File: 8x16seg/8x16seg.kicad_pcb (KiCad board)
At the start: 4 copper layers, 162.2 x 30.5 mm, 76 parts, among them P1 CONN_01X08, P2 CONN_01X08, U1 TLC59282_REV, U2 TLC59282_REV, U3 TLC59282_REV, U4 TLC59282_REV, U5 TLC59282_REV, U6 TLC59282_REV, U7 TLC59282_REV, U8 TLC59282_REV, U9 TLC59282_REV

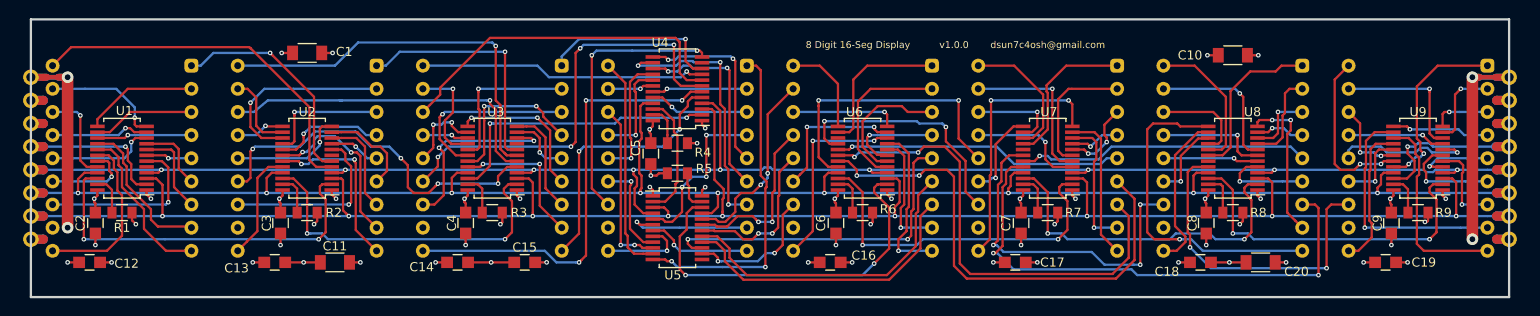
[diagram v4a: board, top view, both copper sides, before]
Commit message: Update 8x16seg design to KiCad 8.
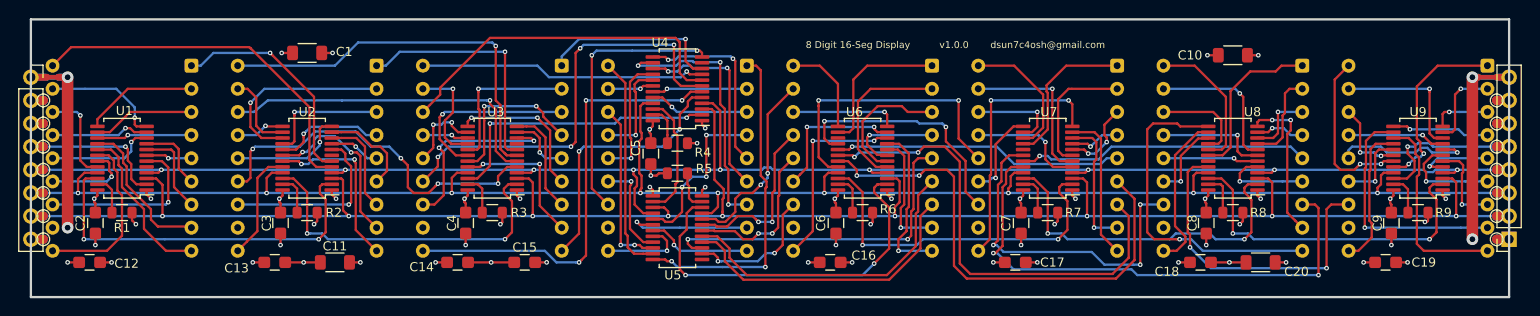
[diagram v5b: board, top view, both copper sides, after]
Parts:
- removed the REF** at (227.1, 97.8) (x2)
- removed the REF** at (227.1, 100.3) (x2)
- removed the REF** at (227.1, 102.9) (x2)
- removed the REF** at (227.1, 105.4) (x2)
- removed the REF** at (227.1, 108.0) (x2)
- removed the REF** at (227.1, 110.5) (x2)
- removed the REF** at (67.6, 110.5) (x2)
- removed the REF** at (227.1, 95.2) (x2)
- removed the REF** at (67.6, 108.0) (x2)
- removed the REF** at (67.6, 105.4) (x2)
- removed the REF** at (67.6, 102.9) (x2)
- removed the REF** at (67.6, 100.3) (x2)
- removed the REF** at (67.6, 97.8) (x2)
- added REF**: TestPoint_Pad_D1.0mm, TestPoint:TestPoint_Pad_D1.0mm, F.Cu at (227.1, 108.0)
- added REF**: TestPoint_Pad_D1.0mm, TestPoint:TestPoint_Pad_D1.0mm, F.Cu at (227.1, 100.3)
- added REF**: TestPoint_Pad_D1.0mm, TestPoint:TestPoint_Pad_D1.0mm, F.Cu at (67.6, 105.4)
- added REF**: TestPoint_Pad_D1.0mm, TestPoint:TestPoint_Pad_D1.0mm, F.Cu at (67.6, 102.9)
- added REF**: TestPoint_Pad_D1.0mm, TestPoint:TestPoint_Pad_D1.0mm, F.Cu at (67.6, 97.8)
- added REF**: TestPoint_Pad_D1.0mm, TestPoint:TestPoint_Pad_D1.0mm, B.Cu at (67.6, 110.5)
- added REF**: TestPoint_Pad_D1.0mm, TestPoint:TestPoint_Pad_D1.0mm, B.Cu at (67.6, 105.4)
- added REF**: TestPoint_Pad_D1.0mm, TestPoint:TestPoint_Pad_D1.0mm, B.Cu at (67.6, 97.8)
- added REF**: TestPoint_Pad_D1.0mm, TestPoint:TestPoint_Pad_D1.0mm, B.Cu at (227.1, 102.9)
- added REF**: TestPoint_Pad_D1.0mm, TestPoint:TestPoint_Pad_D1.0mm, F.Cu at (227.1, 105.4)
- added REF**: TestPoint_Pad_D1.0mm, TestPoint:TestPoint_Pad_D1.0mm, B.Cu at (67.6, 100.3)
- added REF**: TestPoint_Pad_D1.0mm, TestPoint:TestPoint_Pad_D1.0mm, B.Cu at (227.1, 110.5)
- added REF**: TestPoint_Pad_D1.0mm, TestPoint:TestPoint_Pad_D1.0mm, B.Cu at (227.1, 97.8)
- added REF**: TestPoint_Pad_D1.0mm, TestPoint:TestPoint_Pad_D1.0mm, B.Cu at (227.1, 95.2)
- added REF**: TestPoint_Pad_D1.0mm, TestPoint:TestPoint_Pad_D1.0mm, B.Cu at (227.1, 108.0)
- added REF**: TestPoint_Pad_D1.0mm, TestPoint:TestPoint_Pad_D1.0mm, B.Cu at (227.1, 105.4)
- added REF**: TestPoint_Pad_D1.0mm, TestPoint:TestPoint_Pad_D1.0mm, B.Cu at (67.6, 108.0)
- added REF**: TestPoint_Pad_D1.0mm, TestPoint:TestPoint_Pad_D1.0mm, B.Cu at (67.6, 102.9)
- added REF**: TestPoint_Pad_D1.0mm, TestPoint:TestPoint_Pad_D1.0mm, B.Cu at (227.1, 100.3)
- added REF**: TestPoint_Pad_D1.0mm, TestPoint:TestPoint_Pad_D1.0mm, F.Cu at (227.1, 102.9)
- added REF**: TestPoint_Pad_D1.0mm, TestPoint:TestPoint_Pad_D1.0mm, F.Cu at (227.1, 110.5)
- added REF**: TestPoint_Pad_D1.0mm, TestPoint:TestPoint_Pad_D1.0mm, F.Cu at (67.6, 110.5)
- added REF**: TestPoint_Pad_D1.0mm, TestPoint:TestPoint_Pad_D1.0mm, F.Cu at (227.1, 95.2)
- added REF**: TestPoint_Pad_D1.0mm, TestPoint:TestPoint_Pad_D1.0mm, F.Cu at (67.6, 108.0)
- added REF**: TestPoint_Pad_D1.0mm, TestPoint:TestPoint_Pad_D1.0mm, F.Cu at (227.1, 97.8)
- added REF**: TestPoint_Pad_D1.0mm, TestPoint:TestPoint_Pad_D1.0mm, F.Cu at (67.6, 100.3)
- C1, C10, C11, C20: footprint local:C_1206_HandSoldering -> Local:C_1206_HandSoldering
- C12, C13, C14, C15, C16, C17, C18, C19, C2, C3, C4, C5, C6, C7, C8, C9: footprint local:C_0805_HandSoldering -> Local:C_0805_HandSoldering
- DS1, DS2, DS3, DS4, DS5, DS6, DS7, DS8: footprint local:PSA08-11SRWA -> Local:PSA08-11SRWA
- R1, R2, R3, R4, R5, R6, R7, R8, R9: footprint local:R_0805_HandSoldering -> Local:R_0805_HandSoldering
- U1, U2, U3, U4, U5, U6, U7, U8, U9: footprint local:SSOP-24_3.9x8.65mm_Pitch0.635mm -> Local:SSOP-24_3.9x8.65mm_Pitch0.635mm
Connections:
- U1 pad 5: Net-(U1-Pad5) -> unconnected-(U1-OUT0-Pad5)
- U2 pad 7: Net-(U2-Pad7) -> unconnected-(U2-OUT2-Pad7)
- U3 pad 9: Net-(U3-Pad9) -> unconnected-(U3-OUT4-Pad9)
- U4 pad 11: Net-(U4-Pad11) -> unconnected-(U4-OUT6-Pad11)
- U5 pad 13: Net-(U5-Pad13) -> unconnected-(U5-OUT8-Pad13)
- U6 pad 15: Net-(U6-Pad15) -> unconnected-(U6-OUT10-Pad15)
- U7 pad 17: Net-(U7-Pad17) -> unconnected-(U7-OUT12-Pad17)
- U8 pad 19: Net-(U8-Pad19) -> unconnected-(U8-OUT14-Pad19)
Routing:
- net VAA: track 66.9 -> 79.0 mm
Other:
- net class Default removed
- net class minimum removed
- rule solder_mask_min_width: 0.25 -> 0.1016

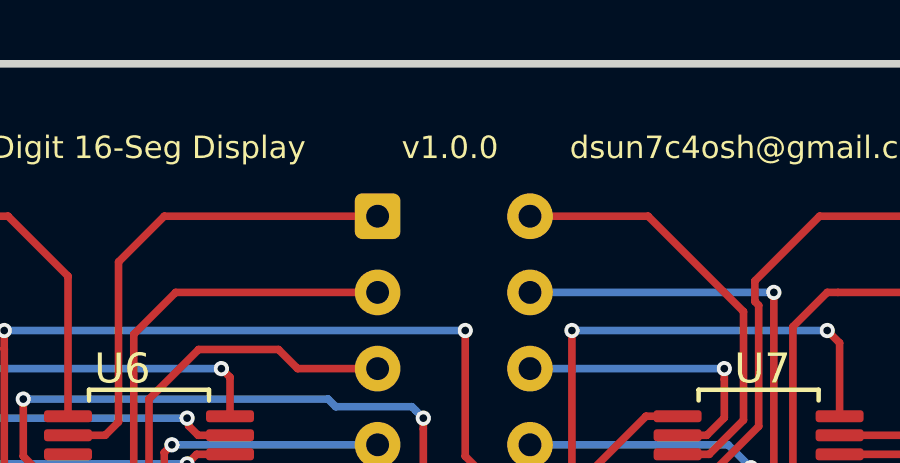
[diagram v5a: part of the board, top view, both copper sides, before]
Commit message: Bump version string of 8x16seg to v1.1.0.
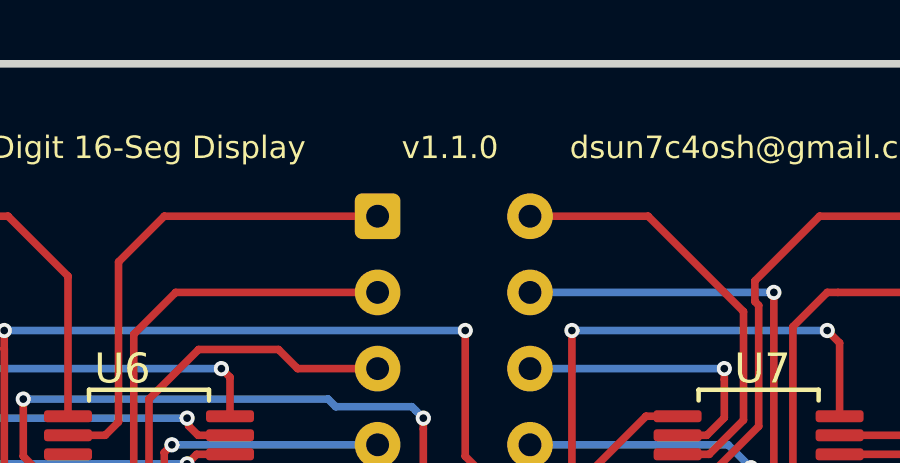
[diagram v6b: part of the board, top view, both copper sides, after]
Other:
- board text added: "v1.1.0"
- board text removed: "v1.0.0"
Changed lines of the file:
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@@
 	(title_block
 		(title "8 Digit 16-Segment Display")
-		(date "2019-12-12")
-		(rev "v1.0.0")
+		(date "2025-01-27")
+		(rev "v1.1.0")
 	)
 	(layers
@@
 			)
 		)
-		(property "Description" ""
+		(property "Description" "16-Channel, Constant-Current LED Driver"
 			(at 0 0 180)
 			(layer "F.Fab")
@@
 			)
 		)
-		(property "Description" ""
+		(property "Description" "16-Channel, Constant-Current LED Driver"
 			(at 0 0 180)
 			(layer "F.Fab")
@@
 			)
 		)
-		(property "Description" ""
+		(property "Description" "16-Channel, Constant-Current LED Driver"
 			(at 0 0 180)
 			(layer "F.Fab")
@@
 			)
 		)
-		(property "Description" ""
+		(property "Description" "16-Channel, Constant-Current LED Driver"
 			(at 0 0 0)
 			(layer "F.Fab")
@@
 			)
 		)
-		(property "Description" ""
+		(property "Description" "16-Channel, Constant-Current LED Driver"
 			(at 0 0 180)
 			(layer "F.Fab")
@@
 			)
 		)
-		(property "Description" ""
+		(property "Description" "16-Channel, Constant-Current LED Driver"
 			(at 0 0 180)
 			(layer "F.Fab")
@@
 			)
 		)
-		(property "Description" ""
+		(property "Description" "16-Channel, Constant-Current LED Driver"
 			(at 0 0 180)
 			(layer "F.Fab")
@@
 			)
 		)
-		(property "Description" ""
+		(property "Description" "16-Channel, Constant-Current LED Driver"
 			(at 0 0 180)
 			(layer "F.Fab")
@@
 			)
 		)
-		(property "Description" ""
+		(property "Description" "16-Channel, Constant-Current LED Driver"
 			(at 0 0 180)
 			(layer "F.Fab")
@@
 			)
 		)
+		(property "Voltage" ""
+			(at 0 0 180)
+			(unlocked yes)
+			(layer "F.Fab")
+			(hide yes)
+			(effects
+				(font
+					(size 1 1)
+					(thickness 0.15)
+				)
+			)
+		)
+		(property "Tolerance" ""
+			(at 0 0 180)
+			(unlocked yes)
+			(layer "F.Fab")
+			(hide yes)
+			(effects
+				(font
+					(size 1 1)
+					(thickness 0.15)
+				)
+			)
+		)
+		(property "Dielectric" ""
+			(at 0 0 180)
+			(unlocked yes)
+			(layer "F.Fab")
+			(hide yes)
+			(effects
+				(font
+					(size 1 1)
+					(thickness 0.15)
+				)
+			)
+		)
+		(property "Power" ""
+			(at 0 0 180)
+			(unlocked yes)
+			(layer "F.Fab")
+			(hide yes)
+			(effects
+				(font
+					(size 1 1)
+					(thickness 0.15)
+				)
+			)
+		)
+		(property "Current" ""
+			(at 0 0 180)
+			(unlocked yes)
+			(layer "F.Fab")
+			(hide yes)
+			(effects
+				(font
+					(size 1 1)
+					(thickness 0.15)
+				)
+			)
+		)
+		(property "Frequency" ""
+			(at 0 0 180)
+			(unlocked yes)
+			(layer "F.Fab")
+			(hide yes)
+			(effects
+				(font
+					(size 1 1)
+					(thickness 0.15)
+				)
+			)
+		)
 		(sheetname "Root")
 		(sheetfile "8x16seg.kicad_sch")
@@
 			)
 		)
-		(property "Description" ""
+		(property "Description" "0.80\" 16 Segment Single Digit Display"
 			(at 0 0 180)
 			(layer "F.Fab")
@@
 			)
 		)
-		(property "Description" ""
+		(property "Description" "0.80\" 16 Segment Single Digit Display"
 			(at 0 0 180)
 			(layer "F.Fab")
@@
 			)
 		)
-		(property "Description" ""
+		(property "Description" "0.80\" 16 Segment Single Digit Display"
 			(at 0 0 180)
 			(layer "F.Fab")
@@
 			)
 		)
-		(property "Description" ""
+		(property "Description" "0.80\" 16 Segment Single Digit Display"
 			(at 0 0 180)
 			(layer "F.Fab")
@@
 			)
 		)
-		(property "Description" ""
+		(property "Description" "0.80\" 16 Segment Single Digit Display"
 			(at 0 0 180)
 			(layer "F.Fab")
@@
 			)
 		)
-		(property "Description" ""
+		(property "Description" "0.80\" 16 Segment Single Digit Display"
 			(at 0 0 180)
 			(layer "F.Fab")
@@
 			)
 		)
-		(property "Description" ""
+		(property "Description" "0.80\" 16 Segment Single Digit Display"
 			(at 0 0 180)
 			(layer "F.Fab")
@@
 			)
 		)
-		(property "Description" ""
+		(property "Description" "0.80\" 16 Segment Single Digit Display"
 			(at 0 0 180)
 			(layer "F.Fab")
@@
 			)
 		)
+		(property "Voltage" ""
+			(at 0 0 180)
+			(unlocked yes)
+			(layer "B.Fab")
+			(hide yes)
+			(effects
+				(font
+					(size 1 1)
+					(thickness 0.15)
+				)
+				(justify mirror)
+			)
+		)
+		(property "Tolerance" ""
+			(at 0 0 180)
+			(unlocked yes)
+			(layer "B.Fab")
+			(hide yes)
+			(effects
+				(font
+					(size 1 1)
+					(thickness 0.15)
+				)
+				(justify mirror)
+			)
+		)
+		(property "Dielectric" ""
+			(at 0 0 180)
+			(unlocked yes)
+			(layer "B.Fab")
+			(hide yes)
+			(effects
+				(font
+					(size 1 1)
+					(thickness 0.15)
+				)
+				(justify mirror)
+			)
+		)
+		(property "Power" ""
+			(at 0 0 180)
+			(unlocked yes)
+			(layer "B.Fab")
+			(hide yes)
+			(effects
+				(font
+					(size 1 1)
+					(thickness 0.15)
+				)
+				(justify mirror)
+			)
+		)
+		(property "Current" ""
+			(at 0 0 180)
+			(unlocked yes)
+			(layer "B.Fab")
+			(hide yes)
+			(effects
+				(font
+					(size 1 1)
+					(thickness 0.15)
+				)
+				(justify mirror)
+			)
+		)
+		(property "Frequency" ""
+			(at 0 0 180)
+			(unlocked yes)
+			(layer "B.Fab")
+			(hide yes)
+			(effects
+				(font
+					(size 1 1)
+					(thickness 0.15)
+				)
+				(justify mirror)
+			)
+		)
 		(property ki_fp_filters "PSA08-11SRWA*")
 		(sheetname "Root")
@@
 		(layer "Edge.Cuts")
 	)
-	(gr_text "v1.0.0"
+	(gr_text "v1.1.0"
 		(at 167.513 89.154 0)
 		(layer "F.SilkS")
